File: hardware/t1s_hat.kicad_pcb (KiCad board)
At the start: 4 copper layers, 66.2 x 49.2 mm, 42 parts, among them CN1 T1S BUS P N N P, J1 2x20 socket (riser stack), U1 LAN8651, Y1 25.000MHz CL12

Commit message: Review follow-ups: GEOMETRY split, BOM/doc consistency, CMC void check, DRC clean, UDP sink
- mechanical/GEOMETRY.md now describes this board only (66.22 x 49.19, no
  notch, 4 holes); the old adapter's outline/notch/6 holes move to
  legacy_adapter_geometry.md
- L1 documented as the 200 uH ACT1210L-201 actually fitted (prototype
  alternative, EMC validation pending); R1/R2 documented as 0.75 W
  substitute for AN1718's 1 W; C4 marked PROTOTYPE_X7R in ORDERING.md
- clock section names the load caps C15/C16 (C1/C2 are the bus caps);
  status LEDs marked as firmware mapping pending
- CMC void forbids tracks on In1/In2/B.Cu; the verifier fails on any
  track or via there, and on F.Cu on anything but L1's nets and the
  known VDDA dogleg (queued for Rev C with test pads and a film CCOMP land)
- NPTH_2.75mm footprint saved to the project library: DRC 0/0/0
- firmware: UDP discard sink on port 9 with a 'sink' command, so blast's
  delivered rate is measured on the far node

Copper, drills and Gerbers are unchanged from Rev B.
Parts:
- R1, R2: value 49R9 1% 1W (DNP) -> 49R9 1% (DNP)

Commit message: Rev C: drop the LEDs the LAN8651 cannot drive, route VDDA clear of the choke, status on the Elite LED
- LAN8651 PADCTRL A0SEL/A1SEL are event capture/generator only - no LED
  function - so D1/D2/R8/R9 go (two extended parts fewer) and DIOA0/1 are
  grounded with DIOA2/3/4
- VDDA leaves pin 29 by two vias under the top lanes instead of running
  0.25 mm inside L1's outline; the CMC-void check needs no exception now
- firmware: Elite LED (IO38) shows PLCA state from PLCA_STS (solid / fast
  blink / slow blink)
- docs: Rev C changes and what was deliberately not done (no DIP/term
  switch, no film CCOMP - none exists in SMD), measured numbers from a
  LAN8651 HAT on this firmware, bring-up order; DRC 0/0/0, CPL check 0 off
Rev B stays at tag rev-b.
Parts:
- removed D1: GRN, LED_SMD:LED_0603_1608Metric
- removed D2: YEL, LED_SMD:LED_0603_1608Metric
- removed R8, R9: 1k, Resistor_SMD:R_0603_1608Metric
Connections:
- U1 pad 18: LED0_K -> GND
- U1 pad 19: LED1_K -> GND
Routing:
- net LED1_K: track 13.0 -> 0.00 mm
- net LED0_K: track 11.0 -> 0.00 mm
- net GND: track 36.8 -> 39.5 mm
- net +3V3: track 10.2 -> 8.05 mm, vias 10 -> 8
- net LED1_A: track 1.89 -> 0.00 mm
- net LED0_A: track 1.89 -> 0.00 mm
- net VDDA: track 10.8 -> 10.5 mm, vias 0 -> 2
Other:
- board text added: "REV C"
- board text removed: "LED0 DIOA0"
- board text removed: "LED1 DIOA1"

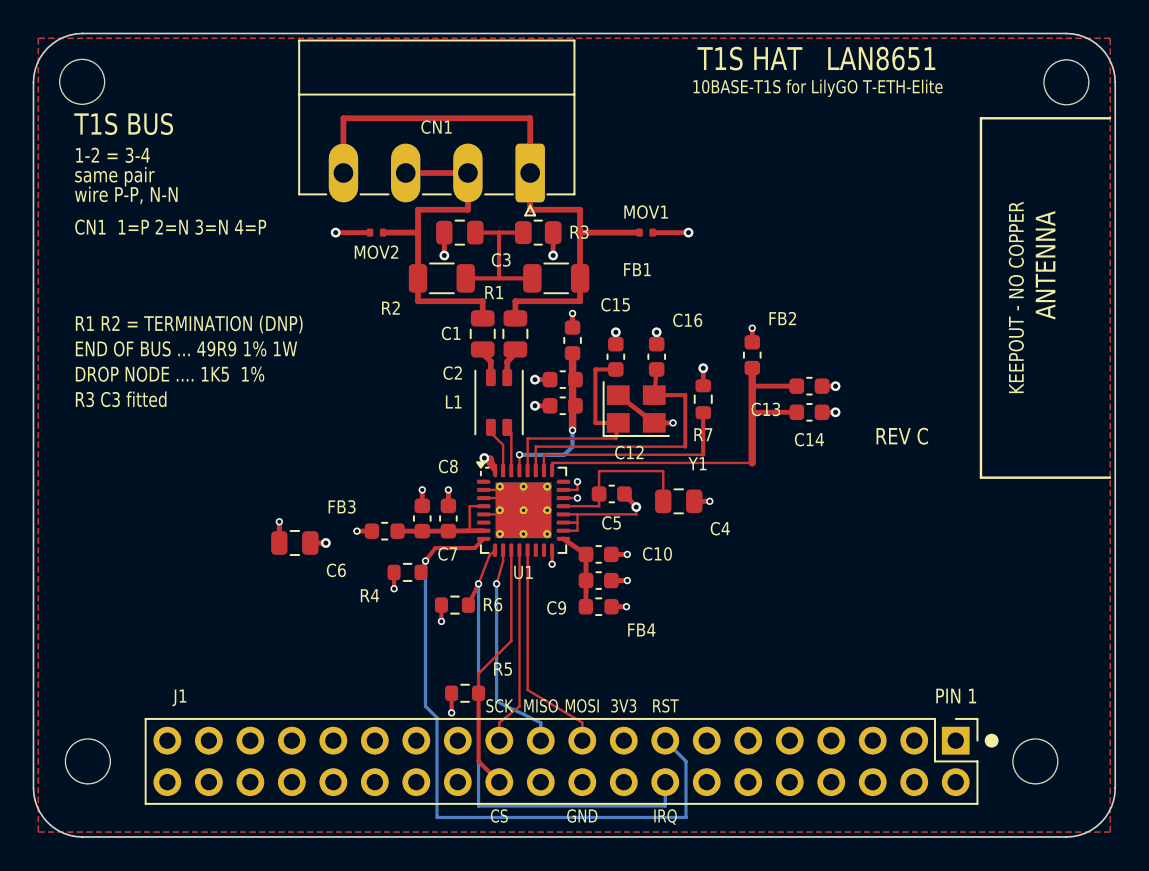
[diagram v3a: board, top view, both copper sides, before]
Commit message: Rev C review fixes: decoupling, RBIAS and crystal at their pins, EP paste clear of vias
Pre-fabrication review of the Rev C layout. Still Rev C; not ordered.

- CCOMP: C5 1.4 mm and C4 2.9 mm from pin 21 (were 2.3 / 6.1 mm), trace
  0.30/0.40 mm and 3.0 mm long (was 0.15 mm, 10.1 mm), own ground vias.
  DIOA0..4 tie inward to the exposed pad to free U1's right edge.
- U1 exposed-pad paste: project-local copy of the TQFN-32 footprint with the
  paste split into 12 windows, each >= 0.15 mm off every thermal via land
  (51 % coverage); land, mask and vias unchanged. Asserted by the verifier.
- VDDAU: C14/C13 2.1/2.6 mm from pin 25 (were 15.4/15.8 mm).
- VDDA: C12 5.0 mm of copper from pin 29 (was 7.1), B.Cu hop now to the
  top-left corner, still clear of the choke void.
- RBIAS: R7 on end beside pin 26, 1.8 mm trace (was 13.3 mm); RBIAS runs
  within 0.6 mm of XTI for 1.4 mm instead of ~10 mm.
- Crystal: XTI 15.7 -> 10.0 mm, XTO 8.3 -> 8.5 mm, load caps at the pads.
- Bus spacing: custom DRC rule BUS_P/BUS_N >= 0.45 mm to any other net
  (t1s_hat.kicad_dru); lanes and MOV stubs adjusted to pass. Net classes
  now really reach the board (0.2 mm, board net names) and the comment that
  claimed otherwise is corrected.
- Silkscreen at J1: "PIN 1 = USB-C END", "TURNED 180 = GND ON 5V".
- erc.rpt regenerated (was Rev B); ELECTRICAL.md: DS60001734F 8.6 gives the
  oscillator gm (18.2 mS nominal, ~16x margin).

DRC 0/0/0 after fill, ERC 0 errors, mechanical error 0, JLC CPL check 0 off
for end/drop/base. Gerbers, drill, BOM/CPL, previews and 3D model rebuilt.
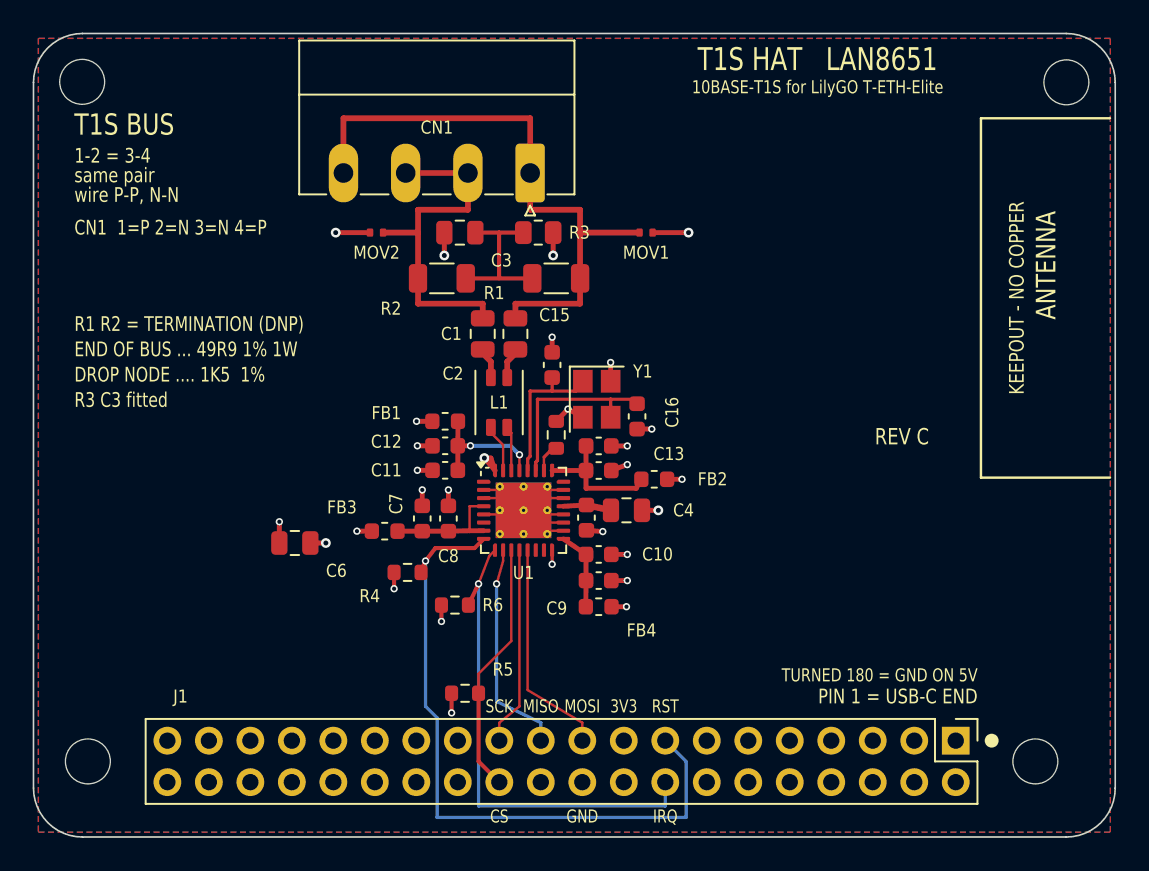
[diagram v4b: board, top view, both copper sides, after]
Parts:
- U1: footprint Package_DFN_QFN:TQFN-32-1EP_5x5mm_P0.5mm_EP3.4x3.4mm_ThermalVias -> t1s_hat:TQFN-32-1EP_5x5mm_P0.5mm_EP3.4x3.4mm_ThermalVias_SplitPaste
- moved C13 13.4 mm to (134.6, 76.1)
- moved C14 13.4 mm to (134.6, 77.6)
- moved FB2 9.68 mm to (138.0, 78.1), turned to 180 degrees
- moved R7 9.26 mm to (132.0, 75.4)
- moved FB1 9.24 mm to (125.2, 74.5), turned to 0 degrees
- moved C11 9.09 mm to (125.2, 77.5)
- moved C12 7.61 mm to (125.2, 76.0)
- moved C15 3.93 mm to (131.8, 71.1)
- moved C16 3.84 mm to (136.9, 74.2), turned to -90 degrees
- moved C4 3.25 mm to (136.3, 80.0)
- moved Y1 2.49 mm to (134.5, 73.2), turned to -90 degrees
- moved C5 2.12 mm to (133.8, 80.5), turned to -90 degrees
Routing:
- net VDDAU: track 24.0 -> 8.37 mm
- net RBIAS: track 13.3 -> 1.75 mm
- net CCOMP: track 10.1 -> 2.95 mm
- net GND: track 39.5 -> 33.0 mm, vias 23 -> 21
- net XTI: track 17.2 -> 11.9 mm
- net XTO: track 14.2 -> 9.29 mm
- net VDDA: track 10.5 -> 7.97 mm
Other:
- board text added: "PIN 1 = USB-C END"
- board text added: "TURNED 180 = GND ON 5V"
- board text removed: "PIN 1"

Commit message: Consistency pass from an audit: docs, schematic notes, one silkscreen line
Board: copper, pads and zones unchanged (347 items compared); the termination silkscreen line
reads '49R9 1%' (the fitted part is 0.75 W, the old line said 1 W). Schematic: title rev C,
clock note CL 12 pF, R1/R2 note >=0.5 W; R3 value 100k 1% (C149504 is 0805W8F1003T5E, F = 1%).
Docs: 6 extended parts with end/drop (5 unfitted), 15 BOM lines, 34 parts, Rev B never
ordered, firmware status = runs on hardware, stale LED/riser/580 KB/partition claims fixed,
min clearance 0.20 and the MOV rule described as written, console list complete (tx, wifi,
ota, zenoh), relative pins.h link, no local paths. DRC 0/0/0, ERC 0 errors, CPL 0 off (x3).
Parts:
- R3: value 100k 5% -> 100k 1%
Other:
- board text added: "END OF BUS ... 49R9 1%"
- board text removed: "END OF BUS ... 49R9 1% 1W"

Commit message: Rev D: push-in spring terminal for the bus (Kefa KF141R-2.54-4P, LCSC C475126) instead of the pluggable Phoenix MC header; pads in two rows, P bridge between them, front/back pads tied on B.Cu; DRC 0, ERC unchanged, JLC CPL exact
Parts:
- CN1: footprint Connector_Phoenix_MC:PhoenixContact_MC_1,5_4-G-3.81_1x04_P3.81mm_Horizontal -> t1s_hat:TerminalBlock_Kefa_KF141R-2.54-4P
- moved CN1 5.27 mm to (126.5, 55.9)
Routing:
- net BUS_N: track 21.8 -> 32.7 mm
- net BUS_P: track 37.6 -> 43.4 mm
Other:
- board text added: "REV D"
- board text removed: "REV C"

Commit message: Rev D: CS off the BOOT strap (header 27 = IO8), DIOA4 1PPS to TP1 and header 13 (IO40)
Review bugs from Rev C. PPS leaves U1 pin 23 through a via and runs on B.Cu;
R5's +3V3 via moved 1 mm left for the CS lane. DRC 0, ERC 0 errors (6 warnings,
DIOA4 no longer grounded), JLC CPL exact.

Firmware: CS found at boot by reading DEVID on IO0 then IO8; ptp pps on drives
the dedicated 1PPS (PADCTRL A4SEL, PPSCTL) and counts edges on IO40. The EG0
path had its registers one too high (0x222.. vs DS60001734F 0x221..); fixed,
now ptp pps eg0 force.
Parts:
- added TP1: PPS, TestPoint:TestPoint_Pad_D1.5mm, F.Cu at (140.0, 88.0)
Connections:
- J1 pad 13: (no net) -> PPS
- J1 pad 24: SPI_CS_N -> (no net)
- J1 pad 27: (no net) -> SPI_CS_N
- U1 pad 23: GND -> PPS
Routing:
- net PPS: track 0.00 -> 23.3 mm, vias 0 -> 2
- net GND: track 33.0 -> 32.2 mm
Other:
- board text added: "PPS"
